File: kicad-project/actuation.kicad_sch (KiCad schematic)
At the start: 44 parts

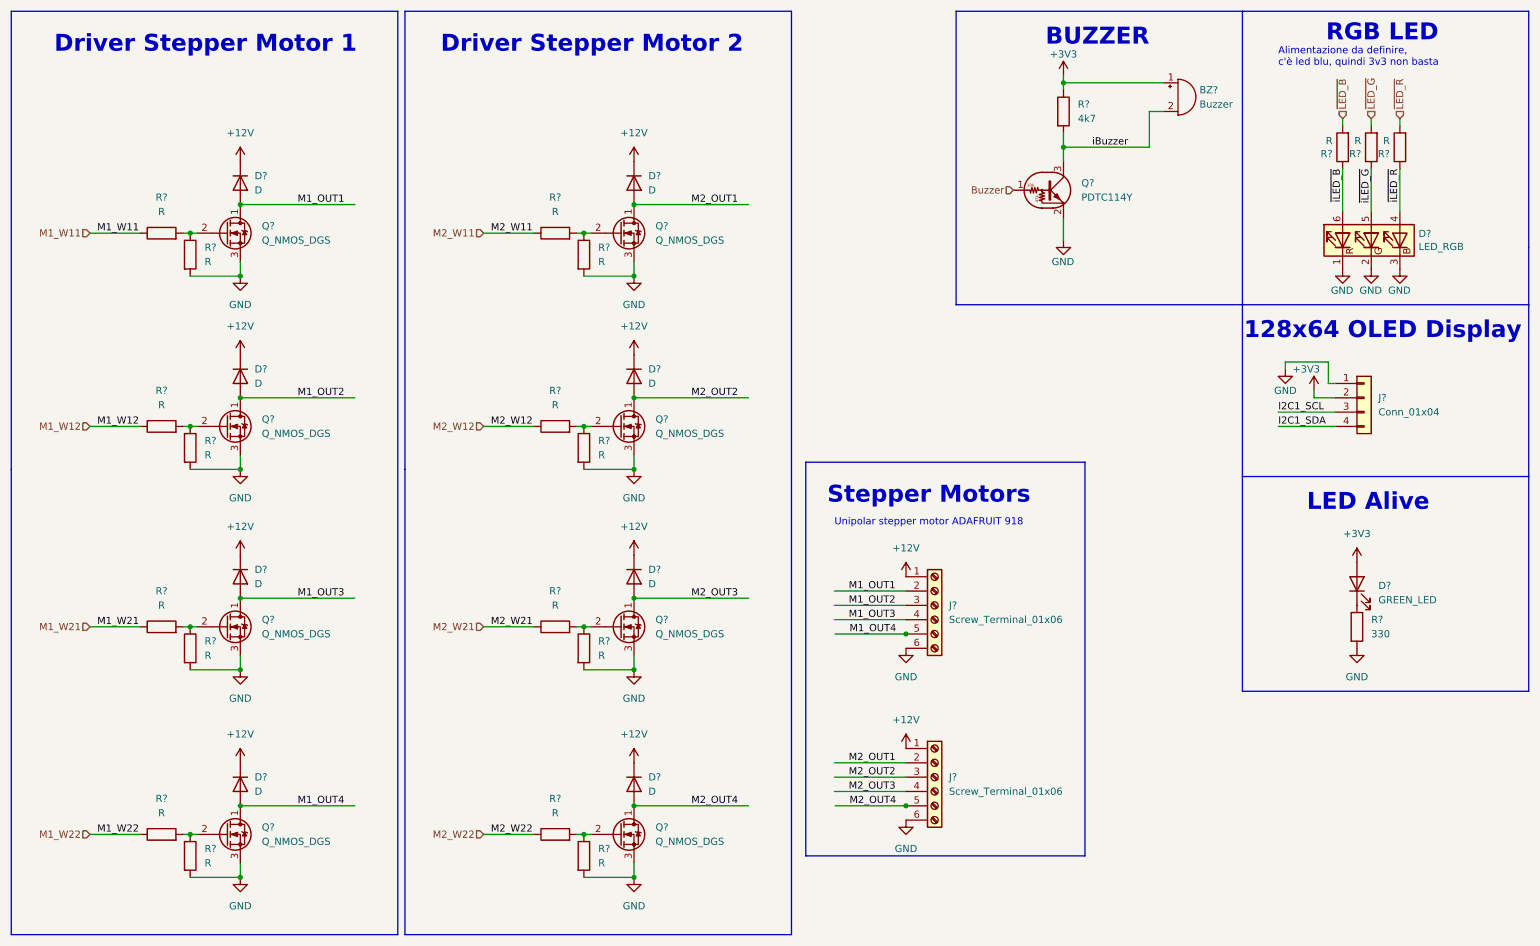
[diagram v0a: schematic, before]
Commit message: hw: add capacitor voltages, fix supply caps and other fixes
add capacitor voltages, change polarized caps to normal, move switching capacitors, remove 5V power, fix switching ballast capacitor, remove switching feedback capacitor, switch sensing and actuation sub-sheets positions in main sheet, add labels to most nodes for pcb layout, connect GPS supply caps directly, remove biased transistor and ferrite bead from GPS enable MOSFET, remove unneeded pins from stepper motors connectors
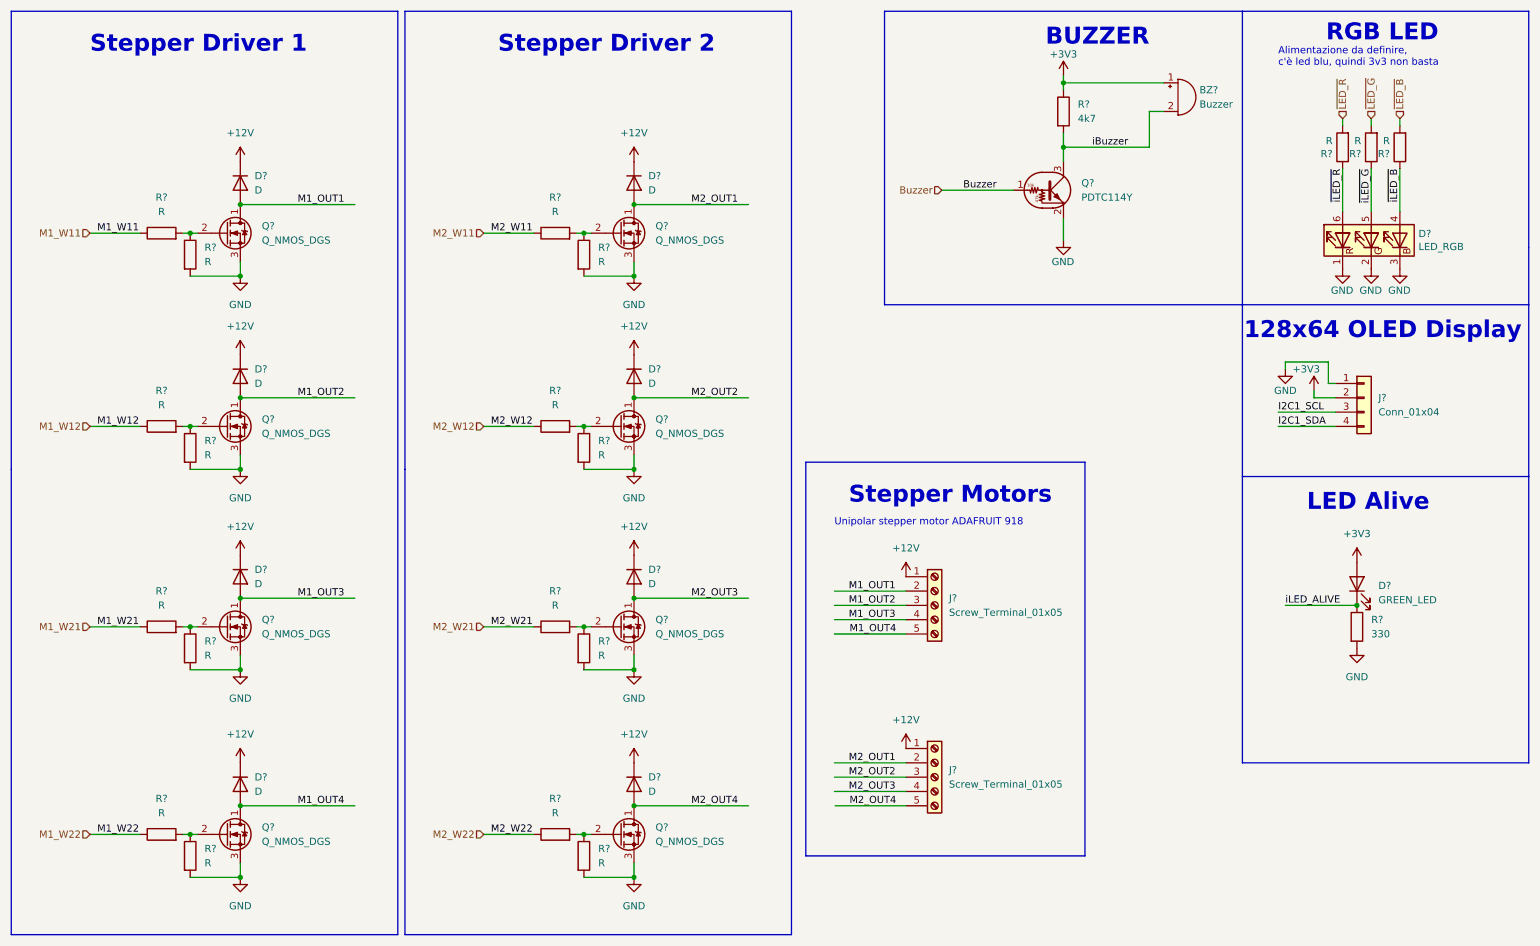
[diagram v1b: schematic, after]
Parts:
- removed J? (x2): Screw_Terminal_01x06, symbol Connector:Screw_Terminal_01x06
- added J? (x2): Screw_Terminal_01x05, symbol Connector:Screw_Terminal_01x05
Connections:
- net +12V: now also J?.1 (Pin_1), J?.1 (Pin_1)
- net M1_OUT1: now also J?.2 (Pin_2)
- net M1_OUT2: now also J?.3 (Pin_3)
- net M1_OUT3: now also J?.4 (Pin_4)
- net M1_OUT4: now also J?.5 (Pin_5)
- net M2_OUT1: now also J?.2 (Pin_2)
- net M2_OUT2: now also J?.3 (Pin_3)
- net M2_OUT3: now also J?.4 (Pin_4)
- net M2_OUT4: now also J?.5 (Pin_5)
- net ~{iLED_B}: now also D?.4 (BA); no longer D?.6 (RA)
- net ~{iLED_R}: now also D?.6 (RA); no longer D?.4 (BA)
- net iLED_ALIVE: now reaches D?.1 (K), R?.1
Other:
- note added: "Stepper Driver 1"
- note added: "Stepper Driver 2"
- note removed: "Driver Stepper Motor 1"
- note removed: "Driver Stepper Motor 2"
- title: (none) -> Actuation
- moved on the sheet: R?
